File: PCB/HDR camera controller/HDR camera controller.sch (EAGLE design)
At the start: 12 parts, among them IC1 USBLC6-4, IC2 RS422-SO8, IC3 RS422-SO8, IC4 RS422-SO8

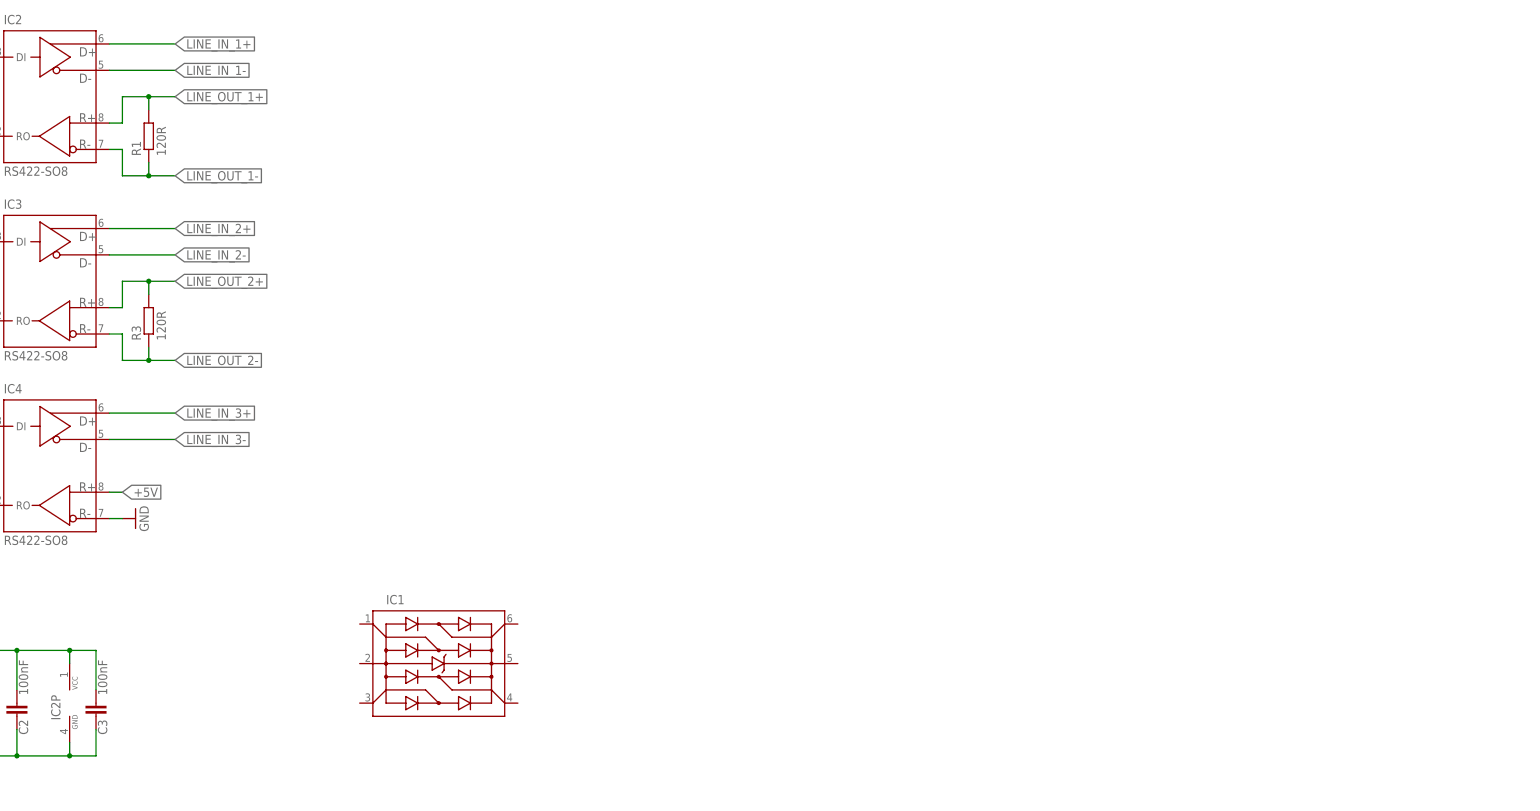
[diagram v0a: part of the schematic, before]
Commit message: schematic update
+USB
+MCU
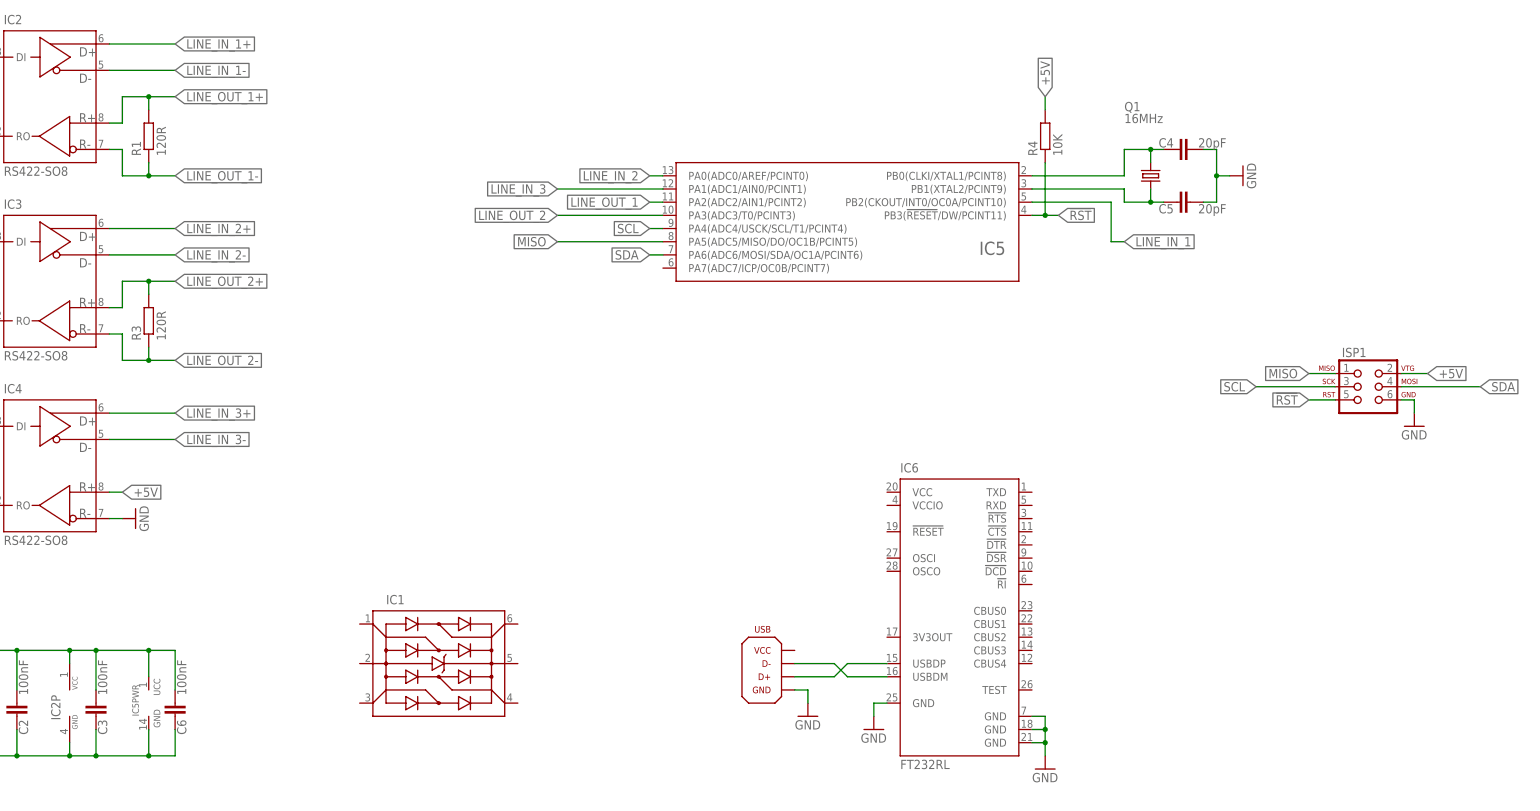
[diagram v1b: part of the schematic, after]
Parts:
- added C4, C5: 20pF, rcl:C-EUC0805
- added C6: 100nF, rcl:C-EUC0805
- added IC5: (no value), atmel_tiny24-44-84tiny48-88mega48-88-168-328:ATTINY24/44/84-SSU
- added IC6: FT232RL, ftdichip:FT232RL
- added ISP1: ISP-SMD, custom connectors:ISP-SMD
- added Q1: 16MHz, crystal:CRYSTALHC49UP
- added R4: 10K, rcl:R-EU_R0805
- added U$1: USB_AB-B_SMD, custom connectors:USB_AB-B_SMD
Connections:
- new net !RST: IC5IC.PB3(!RESET!/DW/PCINT11), ISP1.RST, R4.1
- new net MISO: IC5IC.PA5(ADC5/MISO/DO/OC1B/PCINT5), ISP1.MISO
- new net N$1: C5.2, IC5IC.PB1(XTAL2/PCINT9), Q1.1
- new net N$2: C4.2, IC5IC.PB0(CLKI/XTAL1/PCINT8), Q1.2
- new net N$3: IC6.USBDP, U$1.D+
- new net N$4: IC6.USBDM, U$1.D-
- new net SCL: IC5IC.PA4(ADC4/USCK/SCL/T1/PCINT4), ISP1.SCK
- new net SDA: IC5IC.PA6(ADC6/MOSI/SDA/OC1A/PCINT6), ISP1.MOSI
- net +5V: now also C6.1, IC5PWR.UCC, ISP1.VTG, R4.2
- net GND: now also C4.1, C5.1, C6.2, IC5PWR.GND, IC6.GND, IC6.GND@1, IC6.GND@2, IC6.GND@A, ISP1.GND, U$1.GND
- net LINE_IN_1: now also IC5IC.PB2(CKOUT/INT0/OC0A/PCINT10)
- net LINE_IN_2: now also IC5IC.PA0(ADC0/AREF/PCINT0)
- net LINE_IN_3: now also IC5IC.PA1(ADC1/AIN0/PCINT1)
- net LINE_OUT_1: now also IC5IC.PA2(ADC2/AIN1/PCINT2)
- net LINE_OUT_2: now also IC5IC.PA3(ADC3/T0/PCINT3)

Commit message: trigger controller SW start
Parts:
- added C10, C12, C13, C14, C7, C8, C9: 100nF, rcl:C-EUC0805
- added C11: 100uF, rcl:CPOL-EU153CLV-0810
- added FS1: (no value), custom general:POLYFUSE_1210
- added IC10, IC11, IC9: RS422-SO8, custom ICs:RS422-SO8
- added IC7: 74HC00D, 74xx-eu:74HC00D
- added IC8: 74HC139D, 74xx-eu:74HC139D
- added R7: 10K, rcl:R-EU_R0805
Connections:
- new net B: IC11G$1.DI, IC7C.O
- new net B+: IC11G$1.D+
- new net B-: IC11G$1.D-
- new net G: IC10G$1.DI, IC7B.O
- new net G+: IC10G$1.D+
- new net G-: IC10G$1.D-
- new net N$10: IC7D.I0, IC7D.I1, R7.2
- new net N$11: IC8A.A
- new net N$12: IC8A.B
- new net N$13: FS1.1, U$1.VCC
- new net N$14: C10.2, IC6.3V3OUT
- new net N$5: IC7D.O, IC8A.G
- new net N$6: IC7A.I0, IC8A.Y0
- new net N$7: IC7B.I0, IC8A.Y1
- new net N$8: IC7C.I0, IC8A.Y2
- new net N$9: IC7A.I1, IC7B.I1, IC7C.I1, IC8A.Y3
- new net R: IC7A.O, IC9G$1.DI
- new net R+: IC9G$1.D+
- new net R-: IC9G$1.D-
- net +5V: now also C11.+, C12.1, C13.1, C14.1, C7.1, C8.1, C9.2, FS1.2, IC1.P$5, IC10G$1.R+, IC10P.VCC, IC11G$1.R+, IC11P.VCC, IC6.VCC, IC6.VCCIO, IC7P.VCC, IC8P.VCC, IC9G$1.R+, IC9P.VCC
- net GND: now also C10.1, C11.-, C12.2, C13.2, C14.2, C7.2, C8.2, C9.1, IC1.P$2, IC10G$1.R-, IC10P.GND, IC11G$1.R-, IC11P.GND, IC7P.GND, IC8B.A, IC8B.B, IC8B.G, IC8P.GND, IC9G$1.R-, IC9P.GND, R7.1
- net N$3: now also IC1.P$3
- net N$4: now also IC1.P$1
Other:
- moved on the sheet: C4, C5, IC1, IC2, IC3, IC4, IC5, IC6, ISP1, Q1, R1, R2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

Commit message: develop
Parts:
- removed R6: 10K, rcl:R-EU_R0805
- added C15: 100nF, rcl:C-EUC0805
- added IC12: USBLC6-4, custom ICs:USBLC6-4
- added IC13: (no value), atmel_tiny24-44-84tiny48-88mega48-88-168-328:ATMEGA48/88/168/328-AU
- added LED_PWR, LED_RX, LED_TX: (no value), led:LEDSML0805
- added R10, R11, R12, R8, R9: 1K, rcl:R-EU_R0805
- added R13, R14, R15, R16, R18, R19: 10K, rcl:R-EU_R0805
- added R17: 120R, rcl:R-EU_R0805
- added S1: SWS006, smd-special:SWS006
- R5: value 10K -> 1K
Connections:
- net N$11 renamed RGB_SEL0
- net N$12 renamed RGB_SEL1
- removed net LINE_IN_2: IC3G$1.DI, IC5IC.PA0(ADC0/AREF/PCINT0), R5.2
- removed net LINE_IN_3: IC4G$1.DI, IC5IC.PA1(ADC1/AIN0/PCINT1), R6.2
- removed net SCL: IC5IC.PA4(ADC4/USCK/SCL/T1/PCINT4), ISP1.SCK
- removed net SDA: IC5IC.PA6(ADC6/MOSI/SDA/OC1A/PCINT6), ISP1.MOSI
- new net ENC_A: IC12.P$3, IC3G$1.DI, S1.3, S1.6
- new net ENC_B: IC12.P$1, IC4G$1.DI, S1.2, S1.5
- new net HW_TRIG: IC13IC.PD3(INT1/OC2B/PCINT19)
- new net HW_TRIG+: IC4G$1.R+, R17.2
- new net HW_TRIG-: IC4G$1.R-, R17.1
- new net HW_TRIG_RS: IC4G$1.RO
- new net HW_TRIG_TTL: IC12.P$4, R12.2, S1.1, S1.4
- new net MOSI: IC13IC.PB3(MOSI/OC2A/PCINT3), ISP1.MOSI
- new net N$11: R16.1, S1.9
- new net N$12: R18.1, S1.8
- new net N$15: IC6.TXD, R8.1
- new net N$16: IC6.RXD, R9.1
- new net N$17: C15.2, IC6.!DTR
- new net N$18: IC6.CBUS1, LED_RX.C
- new net N$19: IC6.CBUS0, LED_TX.C
- new net N$20: LED_TX.A, R10.1
- new net N$21: LED_RX.A, R11.1
- new net N$22: R19.1, S1.7
- new net N$23: R15.1, S1.10
- new net N$24: R14.1, S1.11
- new net N$25: R13.1, S1.12
- new net N$26: LED_PWR.A, R5.1
- new net RGB_IN: IC13IC.PD5(T1/OC0B/PCINT21), IC7D.I0, IC7D.I1, R7.2
- new net RX: IC13IC.PD0(RXD/PCINT16), R8.2
- new net SCK: IC13IC.PB5(SCK/PCINT5), ISP1.SCK
- new net TX: IC13IC.PD1(TXD/PCINT17), R9.2
- net !RST: now also C15.1, IC13IC.PC6(!RESET!/PCINT14); no longer IC5IC.PB3(!RESET!/DW/PCINT11)
- net +5V: now also IC12.P$5, IC6.!RESET, R10.2, R11.2, R13.2, R14.2, R15.2, R5.2; no longer IC4G$1.R+
- net GND: now also IC12.P$2, IC6.TEST, LED_PWR.C, R16.2, R18.2, R19.2; no longer IC4G$1.R-, R5.1, R6.1
- net LINE_IN_1: now also IC13IC.PD6(AIN0/OC0A/PCINT22); no longer IC5IC.PB2(CKOUT/INT0/OC0A/PCINT10)
- net LINE_OUT_1: now also IC13IC.PD2(INT0/PCINT18); no longer IC5IC.PA2(ADC2/AIN1/PCINT2)
- net LINE_OUT_2: no longer IC5IC.PA3(ADC3/T0/PCINT3)
- net MISO: now also IC13IC.PB4(MISO/PCINT4); no longer IC5IC.PA5(ADC5/MISO/DO/OC1B/PCINT5)
- net N$1: now also IC13IC.PB6(XTAL1/TOSC1/PCINT6); no longer IC5IC.PB1(XTAL2/PCINT9)
- net N$10: now also R12.1; no longer IC7D.I0, IC7D.I1, R7.2
- net N$2: now also IC13IC.PB7(XTAL2/TOSC2/PCINT7); no longer IC5IC.PB0(CLKI/XTAL1/PCINT8)
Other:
- note added: "Bypass"
- note added: "HW trigger mux"
- note added: "I/O connectors"
- note added: "RGB demux"
- note added: "RS422 drivers"
- note added: "USB <-> TTL"
- moved on the sheet: C1, C10, C11, C12, C13, C14, C2, C3, C4, C5, C6, C7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

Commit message: finished schematic
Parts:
- added C16: 100nF, rcl:C-EUC0805
- added CAM: SMPAD-11, custom connectors:SMPAD-11
- added H1, H2, H3, H4: HOLE-3MM_PLATED, custom mounting:HOLE-3MM_PLATED
- added IC14: 741G157, custom ICs:741G157
- added LIGHT, TRIG: SMPAD-7, custom connectors:SMPAD-7
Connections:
- new net HW_TRIG_SEL: IC13IC.PC2(ADC2/PCINT10), IC14A.!A!/B
- net +5V: now also C16.1, IC14P.VCC, TRIG-1.P
- net B+: now also LIGHT-5.P
- net B-: now also LIGHT-6.P
- net ENC_A: now also IC13IC.PC3(ADC3/PCINT11), TRIG-2.P
- net ENC_B: now also IC13IC.PC4(ADC4/SDA/PCINT12), TRIG-3.P
- net G+: now also LIGHT-3.P
- net G-: now also LIGHT-4.P
- net GND: now also C16.2, CAM-5.P, H1.MOUNT, H2.MOUNT, H3.MOUNT, H4.MOUNT, IC14P.GND, LIGHT-7.P, TRIG-7.P
- net HW_TRIG: now also IC14A.X
- net HW_TRIG+: now also TRIG-5.P
- net HW_TRIG-: now also TRIG-6.P
- net HW_TRIG_RS: now also IC14A.B
- net HW_TRIG_TTL: now also IC14A.A
- net LINE_IN_1+: now also CAM-2.P
- net LINE_IN_1-: now also CAM-1.P
- net LINE_IN_2+: now also CAM-9.P
- net LINE_IN_2-: now also CAM-8.P
- net LINE_IN_3+: now also CAM-4.P
- net LINE_IN_3-: now also CAM-3.P
- net LINE_OUT_1+: now also CAM-7.P
- net LINE_OUT_1-: now also CAM-6.P
- net LINE_OUT_2+: now also CAM-11.P
- net LINE_OUT_2-: now also CAM-10.P
- net N$10: now also TRIG-4.P
- net R+: now also LIGHT-1.P
- net R-: now also LIGHT-2.P
- net RGB_SEL0: now also IC13IC.PC0(ADC0/PCINT8)
- net RGB_SEL1: now also IC13IC.PC1(ADC1/PCINT9)
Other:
- moved on the sheet: C1, C10, C11, C12, C13, C14, C15, C2, C3, C4, C5, C6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

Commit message: PCB WIP
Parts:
- removed IC5: (no value), atmel_tiny24-44-84tiny48-88mega48-88-168-328:ATTINY24/44/84-SSU
- added C17: 100nF, rcl:C-EUC0805
- C11: device rcl:CPOL-EU153CLV-0810 -> rcl:CPOL-EU153CLV-0605
- C4, C5: value 20pF -> 9pF
- Q1: device crystal:CRYSTALHC49UP -> custom passives:RESONATOR_CRY
- renumbered U$1 to USB
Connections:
- new net N$27: C6.1, IC13IC.AREF
- net +5V: now also C17.1, IC13IC.AVCC, IC13PWR.UCC, IC4G$1.R+; no longer C6.1, IC11G$1.R+, IC5PWR.UCC
- net GND: now also C17.2, IC13PWR.GND, IC4G$1.R-; no longer IC11G$1.R-, IC5PWR.GND
- net HW_TRIG+: now also IC11G$1.R+; no longer IC4G$1.R+
- net HW_TRIG-: now also IC11G$1.R-; no longer IC4G$1.R-
- net HW_TRIG_RS: now also IC11G$1.RO; no longer IC4G$1.RO
- net LINE_OUT_2: now also IC13IC.PC5(ADC5/SCL/PCINT13)
- net N$1: now also Q1.2; no longer Q1.1
- net N$2: now also Q1.1; no longer Q1.2
- net N$3: now also IC1.P$1; no longer IC1.P$3
- net N$4: now also IC1.P$3; no longer IC1.P$1
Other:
- moved on the sheet: C1, C12, C13, C14, C16, C2, C3, C6, C7, C8, H1, H2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
